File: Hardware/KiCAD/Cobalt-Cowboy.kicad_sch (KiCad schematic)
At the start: 1 part, among them J3 USB_C_Receptacle

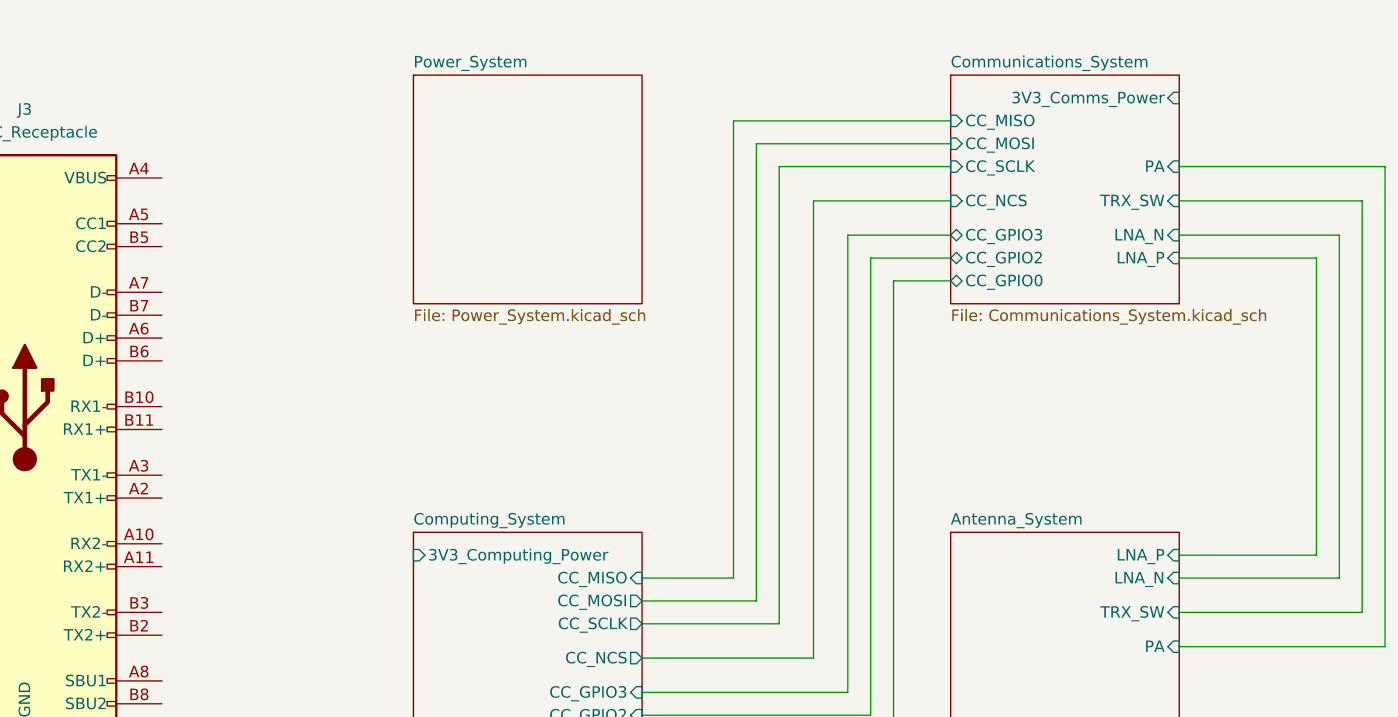
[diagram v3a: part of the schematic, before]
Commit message: feat: corrected Power routing, added TODOs for board, prepared for amps
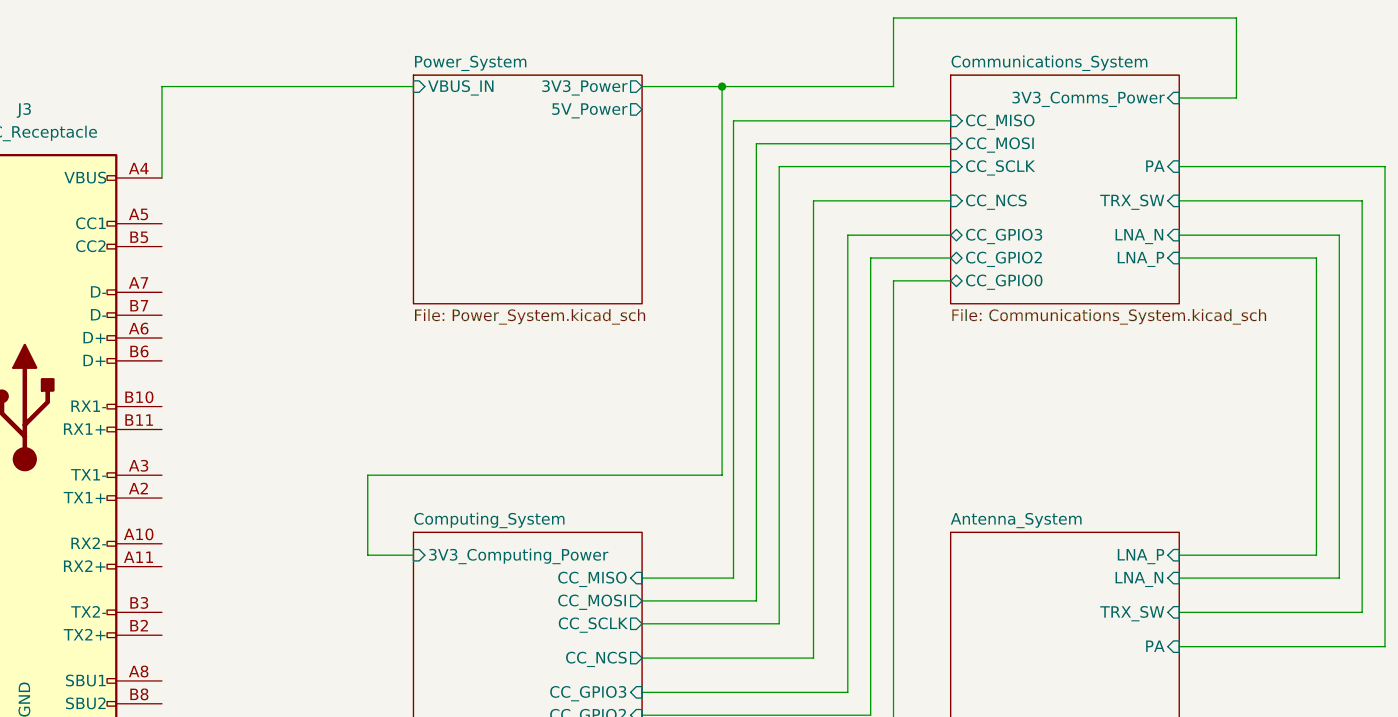
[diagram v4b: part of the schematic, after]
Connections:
- net Power_System/VBUS_IN: now reaches J3.A4 (VBUS), J3.A9 (VBUS), J3.B4 (VBUS), J3.B9 (VBUS)
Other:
- sheet Power_System ports: added 3V3_Power, 5V_Power, VBUS_IN; removed none
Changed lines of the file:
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@@
 (kicad_sch (version 20230121) (generator eeschema)
   (paper "A4")
+  (junction (at 114.3 39.37) (diameter 0) (color 0 0 0 0)
+  )
   (wire (pts (xy 185.42 97.79) (xy 165.1 97.79))
     (stroke (width 0) (type default))
   )
+  (wire (pts (xy 133.35 31.75) (xy 171.45 31.75))
+    (stroke (width 0) (type default))
+  )
+  (wire (pts (xy 74.93 91.44) (xy 80.01 91.44))
+    (stroke (width 0) (type default))
+  )
   (wire (pts (xy 187.96 101.6) (xy 165.1 101.6))
     (stroke (width 0) (type default))
@@
     (stroke (width 0) (type default))
   )
+  (wire (pts (xy 52.07 39.37) (xy 80.01 39.37))
+    (stroke (width 0) (type default))
+  )
   (wire (pts (xy 124.46 52.07) (xy 139.7 52.07))
     (stroke (width 0) (type default))
@@
     (stroke (width 0) (type default))
   )
+  (wire (pts (xy 74.93 82.55) (xy 74.93 91.44))
+    (stroke (width 0) (type default))
+  )
   (wire (pts (xy 182.88 55.88) (xy 182.88 93.98))
     (stroke (width 0) (type default))
   )
+  (wire (pts (xy 133.35 39.37) (xy 133.35 31.75))
+    (stroke (width 0) (type default))
+  )
+  (wire (pts (xy 52.07 49.53) (xy 52.07 39.37))
+    (stroke (width 0) (type default))
+  )
+  (wire (pts (xy 171.45 31.75) (xy 171.45 40.64))
+    (stroke (width 0) (type default))
+  )
   (wire (pts (xy 105.41 106.68) (xy 128.27 106.68))
     (stroke (width 0) (type default))
@@
     (stroke (width 0) (type default))
   )
+  (wire (pts (xy 114.3 39.37) (xy 114.3 82.55))
+    (stroke (width 0) (type default))
+  )
   (wire (pts (xy 124.46 102.87) (xy 124.46 52.07))
     (stroke (width 0) (type default))
@@
     (stroke (width 0) (type default))
   )
+  (wire (pts (xy 114.3 39.37) (xy 133.35 39.37))
+    (stroke (width 0) (type default))
+  )
+  (wire (pts (xy 114.3 82.55) (xy 74.93 82.55))
+    (stroke (width 0) (type default))
+  )
+  (wire (pts (xy 105.41 39.37) (xy 114.3 39.37))
+    (stroke (width 0) (type default))
+  )
   (wire (pts (xy 120.65 48.26) (xy 139.7 48.26))
     (stroke (width 0) (type default))
@@
   )
   (wire (pts (xy 180.34 58.42) (xy 180.34 91.44))
+    (stroke (width 0) (type default))
+  )
+  (wire (pts (xy 171.45 40.64) (xy 165.1 40.64))
     (stroke (width 0) (type default))
   )
@@
       (effects (font (size 1.27 1.27)) (justify left top))
     )
-    (instances
+    (pin "VBUS_IN" input (at 80.01 39.37 180)
+      (effects (font (size 1.27 1.27)) (justify left))
+    )
+    (pin "3V3_Power" output (at 105.41 39.37 0)
+      (effects (font (size 1.27 1.27)) (justify right))
+    )
+    (pin "5V_Power" output (at 105.41 41.91 0)
+      (effects (font (size 1.27 1.27)) (justify right))
+    )
+    (instances

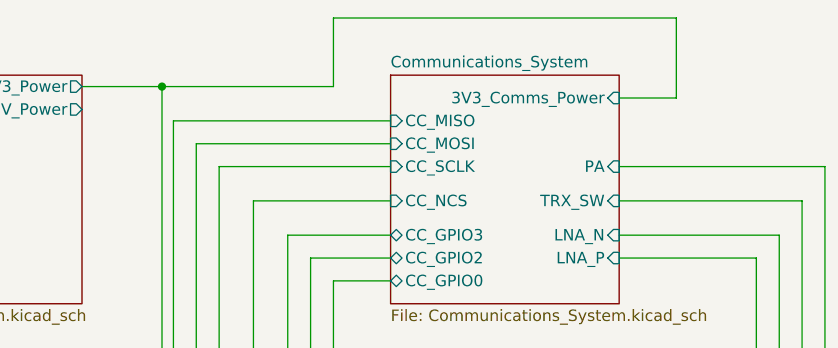
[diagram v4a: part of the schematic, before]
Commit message: added  keypad
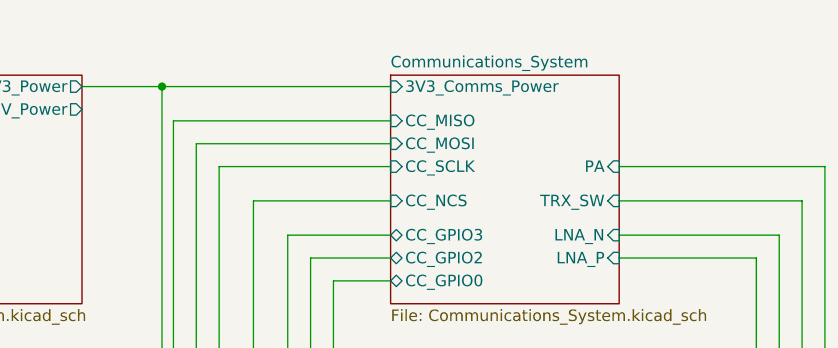
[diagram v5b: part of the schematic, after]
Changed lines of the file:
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@@
-    (stroke (width 0) (type default))
-  )
-  (wire (pts (xy 133.35 31.75) (xy 171.45 31.75))
     (stroke (width 0) (type default))
   )
@@
     (stroke (width 0) (type default))
   )
-  (wire (pts (xy 133.35 39.37) (xy 133.35 31.75))
-    (stroke (width 0) (type default))
-  )
   (wire (pts (xy 52.07 49.53) (xy 52.07 39.37))
     (stroke (width 0) (type default))
   )
-  (wire (pts (xy 171.45 31.75) (xy 171.45 40.64))
-    (stroke (width 0) (type default))
-  )
   (wire (pts (xy 105.41 106.68) (xy 128.27 106.68))
     (stroke (width 0) (type default))
@@
     (stroke (width 0) (type default))
   )
-  (wire (pts (xy 114.3 39.37) (xy 133.35 39.37))
+  (wire (pts (xy 114.3 39.37) (xy 139.7 39.37))
     (stroke (width 0) (type default))
   )
@@
   )
   (wire (pts (xy 180.34 58.42) (xy 180.34 91.44))
-    (stroke (width 0) (type default))
-  )
-  (wire (pts (xy 171.45 40.64) (xy 165.1 40.64))
     (stroke (width 0) (type default))
   )
@@
       (effects (font (size 1.27 1.27)) (justify left))
     )
-    (pin "3V3_Comms_Power" input (at 165.1 40.64 0)
-      (effects (font (size 1.27 1.27)) (justify right))
-    )
-    (instances
+    (pin "3V3_Comms_Power" input (at 139.7 39.37 180)
+      (effects (font (size 1.27 1.27)) (justify left))
+    )
+    (instances

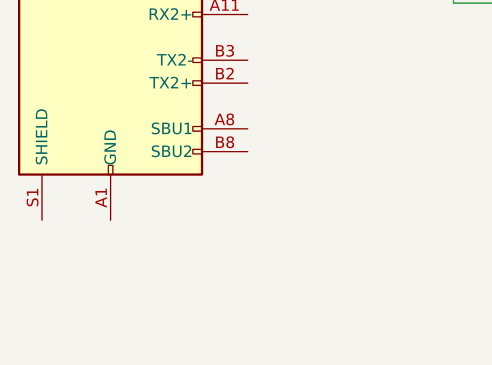
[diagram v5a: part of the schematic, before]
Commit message: Added a GND to USBC connector
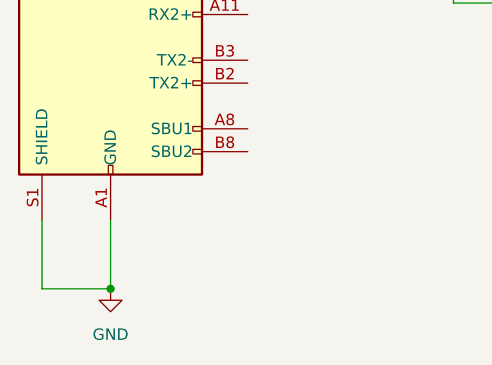
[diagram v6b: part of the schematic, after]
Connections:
- net GND: now reaches J3.A1 (GND), J3.A12 (GND), J3.B1 (GND), J3.B12 (GND)
- net GND: now also J3.S1 (SHIELD)
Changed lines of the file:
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@@
 (kicad_sch (version 20230121) (generator eeschema)
   (paper "A4")
+  (junction (at 36.83 123.19) (diameter 0) (color 0 0 0 0)
+  )
   (junction (at 114.3 39.37) (diameter 0) (color 0 0 0 0)
   )
@@
   )
   (wire (pts (xy 120.65 99.06) (xy 120.65 48.26))
+    (stroke (width 0) (type default))
+  )
+  (wire (pts (xy 29.21 123.19) (xy 36.83 123.19))
+    (stroke (width 0) (type default))
+  )
+  (wire (pts (xy 36.83 115.57) (xy 36.83 123.19))
     (stroke (width 0) (type default))
   )
@@
     (stroke (width 0) (type default))
   )
+  (wire (pts (xy 29.21 115.57) (xy 29.21 123.19))
+    (stroke (width 0) (type default))
+  )
   (wire (pts (xy 128.27 55.88) (xy 139.7 55.88))
     (stroke (width 0) (type default))
@@
     (stroke (width 0) (type default))
   )
+  (symbol (lib_id "power:GND") (at 36.83 123.19 0) (unit 1)
+    (in_bom yes) (on_board yes) (dnp no) (fields_autoplaced)
+    (property "Reference" "#PWR022" (at 36.83 129.54 0)
+      (effects (font (size 1.27 1.27)) hide)
+    )
+    (property "Value" "GND" (at 36.83 128.27 0)
+      (effects (font (size 1.27 1.27)))
+    )
+    (property "Footprint" "" (at 36.83 123.19 0)
+      (effects (font (size 1.27 1.27)) hide)
+    )
+    (property "Datasheet" "" (at 36.83 123.19 0)
+      (effects (font (size 1.27 1.27)) hide)
+    )
+    (pin "1")
+    (instances
+      (project "Cobalt-Cowboy"
+        (path "/60a68eb1-aa0f-414e-b03b-965ad6b52dab"
+          (reference "#PWR022") (unit 1)
+        )
+      )
+    )
+  )
   (symbol (lib_id "Connector:USB_C_Receptacle") (at 36.83 74.93 0) (unit 1)

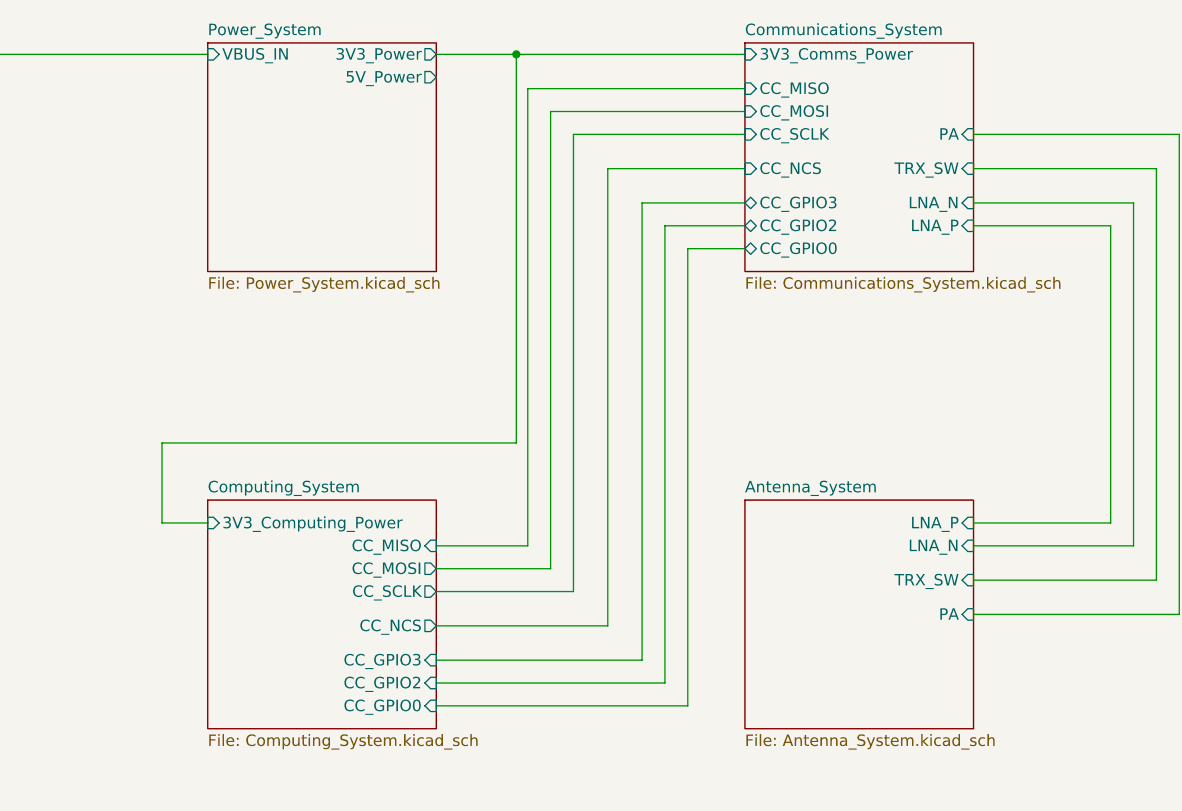
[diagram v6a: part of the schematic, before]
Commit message: Added seperate schematic for amplifier assembly
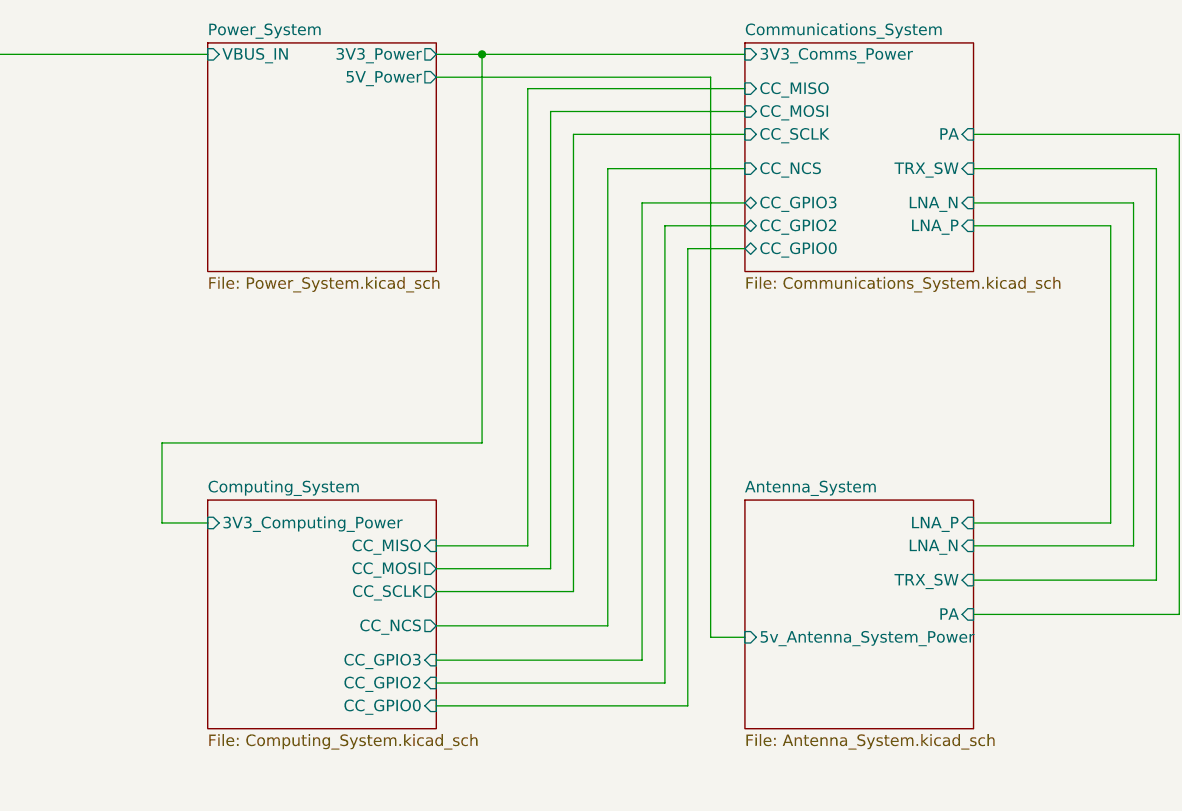
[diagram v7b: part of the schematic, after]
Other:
- sheet Antenna_System ports: added 5v_Antenna_System_Power; removed none
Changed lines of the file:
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@@
   (junction (at 36.83 123.19) (diameter 0) (color 0 0 0 0)
   )
-  (junction (at 114.3 39.37) (diameter 0) (color 0 0 0 0)
+  (junction (at 110.49 39.37) (diameter 0) (color 0 0 0 0)
   )
   (wire (pts (xy 185.42 97.79) (xy 165.1 97.79))
@@
     (stroke (width 0) (type default))
   )
+  (wire (pts (xy 135.89 104.14) (xy 139.7 104.14))
+    (stroke (width 0) (type default))
+  )
   (wire (pts (xy 52.07 39.37) (xy 80.01 39.37))
     (stroke (width 0) (type default))
@@
     (stroke (width 0) (type default))
   )
+  (wire (pts (xy 105.41 41.91) (xy 135.89 41.91))
+    (stroke (width 0) (type default))
+  )
   (wire (pts (xy 105.41 106.68) (xy 128.27 106.68))
     (stroke (width 0) (type default))
@@
     (stroke (width 0) (type default))
   )
+  (wire (pts (xy 135.89 41.91) (xy 135.89 104.14))
+    (stroke (width 0) (type default))
+  )
   (wire (pts (xy 165.1 58.42) (xy 180.34 58.42))
     (stroke (width 0) (type default))
   )
-  (wire (pts (xy 114.3 39.37) (xy 114.3 82.55))
+  (wire (pts (xy 110.49 39.37) (xy 110.49 82.55))
     (stroke (width 0) (type default))
   )
@@
     (stroke (width 0) (type default))
   )
-  (wire (pts (xy 114.3 39.37) (xy 139.7 39.37))
-    (stroke (width 0) (type default))
-  )
-  (wire (pts (xy 114.3 82.55) (xy 74.93 82.55))
-    (stroke (width 0) (type default))
-  )
-  (wire (pts (xy 105.41 39.37) (xy 114.3 39.37))
+  (wire (pts (xy 110.49 39.37) (xy 139.7 39.37))
+    (stroke (width 0) (type default))
+  )
+  (wire (pts (xy 110.49 82.55) (xy 74.93 82.55))
+    (stroke (width 0) (type default))
+  )
+  (wire (pts (xy 105.41 39.37) (xy 110.49 39.37))
     (stroke (width 0) (type default))
   )
@@
     (instances
       (project "Cobalt-Cowboy"
-        (path "/60a68eb1-aa0f-414e-b03b-965ad6b52dab/f41c6f3a-9e23-419e-9eda-91d37d832739"
-          (reference "J3") (unit 1)
-        )
         (path "/60a68eb1-aa0f-414e-b03b-965ad6b52dab"
           (reference "J3") (unit 1)
@@
       (effects (font (size 1.27 1.27)) (justify right))
     )
-    (instances
+    (pin "5v_Antenna_System_Power" input (at 139.7 104.14 180)
+      (effects (font (size 1.27 1.27)) (justify left))
+    )
+    (instances
